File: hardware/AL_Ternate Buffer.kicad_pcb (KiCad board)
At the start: 2 copper layers, 45.7 x 71.1 mm, 0 parts

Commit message: Cursory start to layout.
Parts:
- added BT1: 9V, Connector_PinHeader_2.54mm:PinHeader_2x01_P2.54mm_Vertical, F.Cu at (77.9, 117.6)
- added C1: 47u 35V 20%, Capacitor_SMD:C_2220_5750Metric_Pad1.97x5.40mm_HandSolder, F.Cu at (69.9, 61.4)
- added C10: 100p 50V 5%, Capacitor_SMD:C_0805_2012Metric_Pad1.18x1.45mm_HandSolder, F.Cu at (82.8, 107.8)
- added C11: 100n 100V 10%, Capacitor_SMD:C_0805_2012Metric_Pad1.18x1.45mm_HandSolder, F.Cu at (82.8, 110.8)
- added C12: 100n 100V 10%, Capacitor_SMD:C_0805_2012Metric_Pad1.18x1.45mm_HandSolder, F.Cu at (82.8, 113.8)
- added C13: 10u 25V 10%, Capacitor_SMD:C_0805_2012Metric_Pad1.18x1.45mm_HandSolder, F.Cu at (87.6, 104.8)
- added C14: 10u 25V 10%, Capacitor_SMD:C_0805_2012Metric_Pad1.18x1.45mm_HandSolder, F.Cu at (87.6, 107.8)
- added C15: 10u 25V 10%, Capacitor_SMD:C_0805_2012Metric_Pad1.18x1.45mm_HandSolder, F.Cu at (87.6, 110.8)
- added C16: 10u 25V 10%, Capacitor_SMD:C_0805_2012Metric_Pad1.18x1.45mm_HandSolder, F.Cu at (87.6, 113.8)
- added C17: 10u 75V 10%, Capacitor_SMD:C_1210_3225Metric_Pad1.33x2.70mm_HandSolder, F.Cu at (77.3, 79.0)
- added C18: 10u 75V 10%, Capacitor_SMD:C_1210_3225Metric_Pad1.33x2.70mm_HandSolder, F.Cu at (77.3, 83.3)
- added C2: 47u 35V 20%, Capacitor_SMD:C_2220_5750Metric_Pad1.97x5.40mm_HandSolder, F.Cu at (69.9, 68.3)
- added C3: 47u 35V 20%, Capacitor_SMD:C_2220_5750Metric_Pad1.97x5.40mm_HandSolder, F.Cu at (69.9, 75.3)
- added C4: 10u 25V 10%, Capacitor_SMD:C_0805_2012Metric_Pad1.18x1.45mm_HandSolder, F.Cu at (78.0, 104.8)
- added C5: 1u 50V 10%, Capacitor_SMD:C_0805_2012Metric_Pad1.18x1.45mm_HandSolder, F.Cu at (78.0, 107.8)
- added C6: 47u 35V 20%, Capacitor_SMD:C_2220_5750Metric_Pad1.97x5.40mm_HandSolder, F.Cu at (69.9, 82.2)
- added C7: 10u 25V 10%, Capacitor_SMD:C_0805_2012Metric_Pad1.18x1.45mm_HandSolder, F.Cu at (78.0, 110.8)
- added C8: 1u 50V 10%, Capacitor_SMD:C_0805_2012Metric_Pad1.18x1.45mm_HandSolder, F.Cu at (78.0, 113.8)
- added C9: 100p 50V 5%, Capacitor_SMD:C_0805_2012Metric_Pad1.18x1.45mm_HandSolder, F.Cu at (82.8, 104.8)
- added D1: S3GHE3_A/I, Diode_SMD:D_SMB-SMC_Universal_Handsoldering, F.Cu at (82.1, 89.6)
- added D2: S3GHE3_A/I, Diode_SMD:D_SMB-SMC_Universal_Handsoldering, F.Cu at (82.1, 97.3)
- added D3: QBL8IW60D-NW, LED_THT:LED_D5.0mm, F.Cu at (82.8, 80.6)
- added H1: MountingHole_Pad, MountingHole:MountingHole_2.7mm_M2.5_Pad, F.Cu at (62.0, 61.4)
- added H2: MountingHole_Pad, MountingHole:MountingHole_2.7mm_M2.5_Pad, F.Cu at (62.0, 68.3)
- added H3: MountingHole_Pad, MountingHole:MountingHole_2.7mm_M2.5_Pad, F.Cu at (62.0, 75.3)
- added H4: MountingHole_Pad, MountingHole:MountingHole_2.7mm_M2.5_Pad, F.Cu at (62.0, 82.2)
- added J1: FC68148, Connector_BarrelJack:BarrelJack_Horizontal, F.Cu at (73.1, 108.7)
- added J2: NMJ6HCD2, Connector_Audio:Jack_6.35mm_Neutrik_NMJ6HCD2_Horizontal, F.Cu at (138.5, 76.7)
- added J3: NMJ6HCD2, Connector_Audio:Jack_6.35mm_Neutrik_NMJ6HCD2_Horizontal, F.Cu at (151.0, 82.1)
- added J4: NMJ6HCD2, Connector_Audio:Jack_6.35mm_Neutrik_NMJ6HCD2_Horizontal, F.Cu at (151.0, 103.6)
- added R1: 750, Resistor_SMD:R_0603_1608Metric_Pad0.98x0.95mm_HandSolder, F.Cu at (60.7, 87.0)
- added R10: 1M 1%, Resistor_SMD:R_0603_1608Metric_Pad0.98x0.95mm_HandSolder, F.Cu at (65.1, 92.0)
- added R11: 1k 1%, Resistor_SMD:R_0603_1608Metric_Pad0.98x0.95mm_HandSolder, F.Cu at (65.1, 94.5)
- added R12: 1k 1%, Resistor_SMD:R_0603_1608Metric_Pad0.98x0.95mm_HandSolder, F.Cu at (65.1, 97.0)
- added R13: 1M 1%, Resistor_SMD:R_0603_1608Metric_Pad0.98x0.95mm_HandSolder, F.Cu at (65.1, 99.5)
- added R14: 10k 0.5%, Resistor_SMD:R_0603_1608Metric_Pad0.98x0.95mm_HandSolder, F.Cu at (65.1, 102.0)
- added R15: 10k 0.5%, Resistor_SMD:R_0603_1608Metric_Pad0.98x0.95mm_HandSolder, F.Cu at (69.4, 87.0)
- added R16: 10k 0.5%, Resistor_SMD:R_0603_1608Metric_Pad0.98x0.95mm_HandSolder, F.Cu at (69.4, 89.5)
- added R17: 10k 0.5%, Resistor_SMD:R_0603_1608Metric_Pad0.98x0.95mm_HandSolder, F.Cu at (69.4, 92.0)
- added R18: 0, Resistor_SMD:R_0603_1608Metric_Pad0.98x0.95mm_HandSolder, F.Cu at (69.4, 94.5)
- added R19: 10k 0.5%, Resistor_SMD:R_0603_1608Metric_Pad0.98x0.95mm_HandSolder, F.Cu at (69.4, 97.0)
- added R2: 100 5%, Resistor_SMD:R_0603_1608Metric_Pad0.98x0.95mm_HandSolder, F.Cu at (60.7, 89.5)
- added R20: 10k 0.5%, Resistor_SMD:R_0603_1608Metric_Pad0.98x0.95mm_HandSolder, F.Cu at (69.4, 99.5)
- added R21: 0, Resistor_SMD:R_0603_1608Metric_Pad0.98x0.95mm_HandSolder, F.Cu at (69.4, 102.0)
- added R22: 10k 0.5%, Resistor_SMD:R_0603_1608Metric_Pad0.98x0.95mm_HandSolder, F.Cu at (73.8, 87.0)
- added R23: 10k 0.5%, Resistor_SMD:R_0603_1608Metric_Pad0.98x0.95mm_HandSolder, F.Cu at (73.8, 89.5)
- added R24: 10k 0.5%, Resistor_SMD:R_0603_1608Metric_Pad0.98x0.95mm_HandSolder, F.Cu at (73.8, 92.0)
- added R25: 10k 0.5%, Resistor_SMD:R_0603_1608Metric_Pad0.98x0.95mm_HandSolder, F.Cu at (73.8, 94.5)
- added R3: 100 5%, Resistor_SMD:R_0603_1608Metric_Pad0.98x0.95mm_HandSolder, F.Cu at (60.7, 92.0)
- added R4: 10k 0.5%, Resistor_SMD:R_0603_1608Metric_Pad0.98x0.95mm_HandSolder, F.Cu at (60.7, 94.5)
- added R5: 10k 0.5%, Resistor_SMD:R_0603_1608Metric_Pad0.98x0.95mm_HandSolder, F.Cu at (60.7, 97.0)
- added R6: 10k 0.5%, Resistor_SMD:R_0603_1608Metric_Pad0.98x0.95mm_HandSolder, F.Cu at (60.7, 99.5)
- added R7: 10k 0.5%, Resistor_SMD:R_0603_1608Metric_Pad0.98x0.95mm_HandSolder, F.Cu at (60.7, 102.0)
- added R8: 1k 1%, Resistor_SMD:R_0603_1608Metric_Pad0.98x0.95mm_HandSolder, F.Cu at (65.1, 87.0)
- added R9: 1k 1%, Resistor_SMD:R_0603_1608Metric_Pad0.98x0.95mm_HandSolder, F.Cu at (65.1, 89.5)
- added RV1: 10k A, Potentiometer_THT:Potentiometer_Runtron_RM-065_Vertical, F.Cu at (75.9, 70.4)
- added RV2: 10k A, Potentiometer_THT:Potentiometer_Runtron_RM-065_Vertical, F.Cu at (84.0, 70.4)
- added SW1: 7101SYZQE, Connector_PinHeader_2.54mm:PinHeader_1x03_P2.54mm_Vertical, F.Cu at (85.1, 60.2)
- added U1: OPA1664AIDR, Package_SO:SOIC-14_3.9x8.7mm_P1.27mm, F.Cu at (78.5, 63.2)

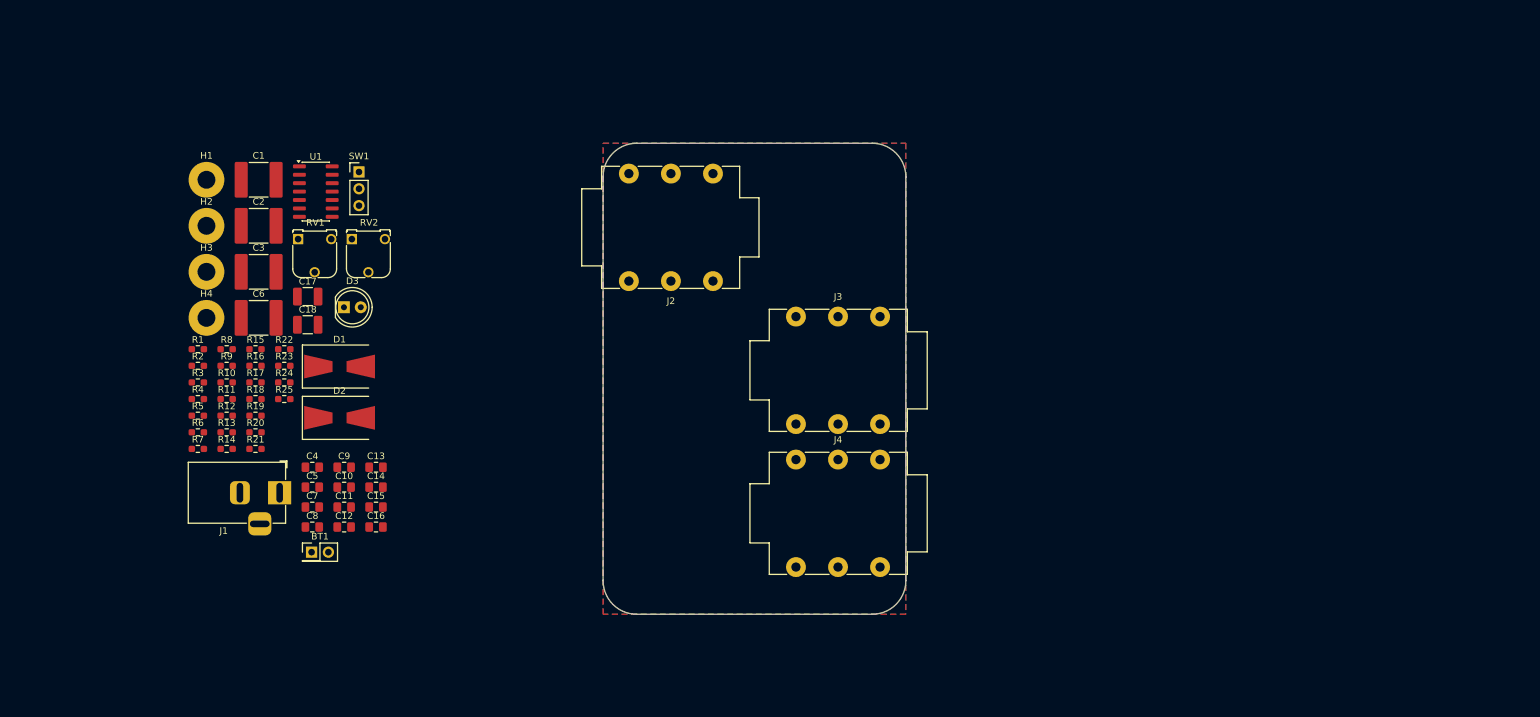
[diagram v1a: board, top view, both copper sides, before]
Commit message: Loose component grouping.
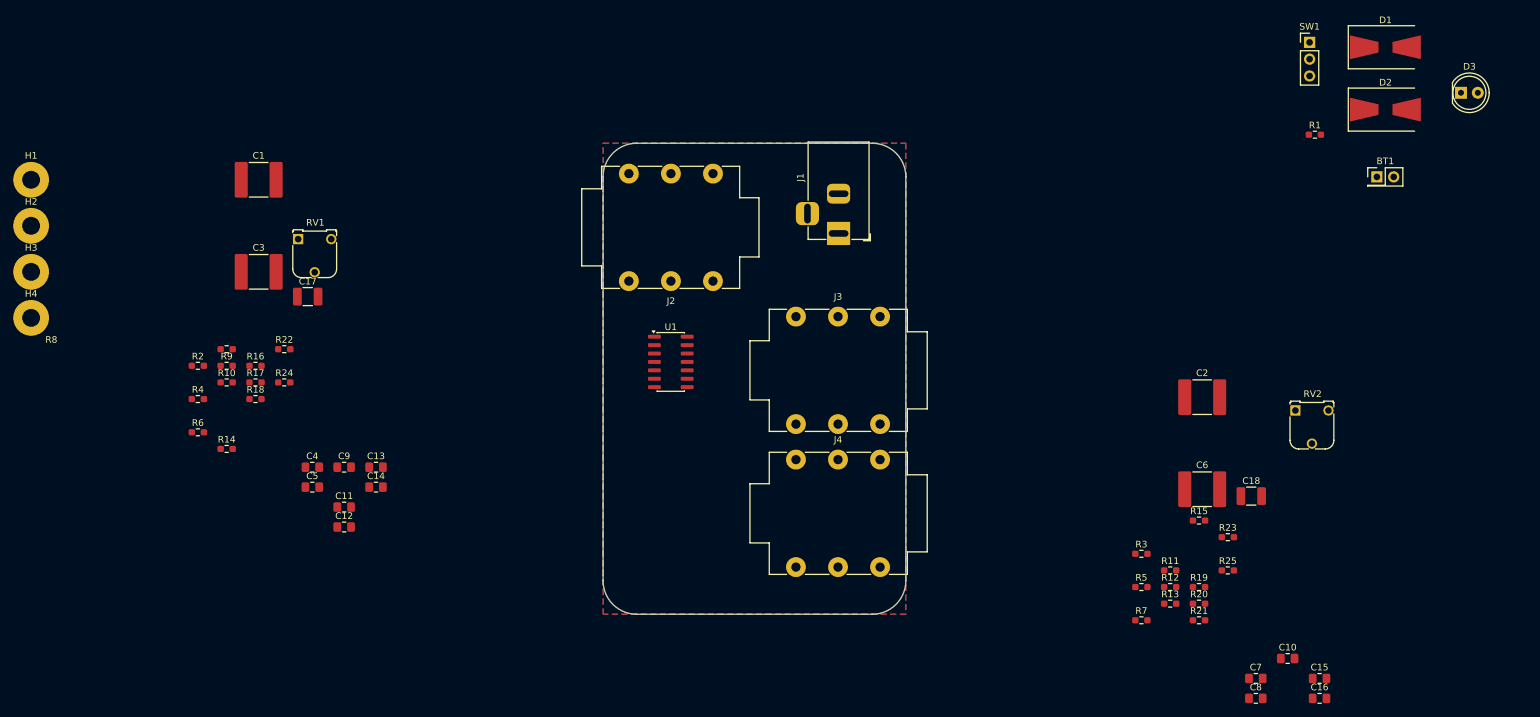
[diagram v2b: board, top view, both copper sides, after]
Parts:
- moved D3 171.7 mm to (251.5, 48.3)
- moved R1 171.7 mm to (229.4, 54.6)
- moved BT1 170.5 mm to (238.8, 61.0)
- moved D1 165.1 mm to (240.1, 41.4)
- moved D2 164.6 mm to (240.1, 50.8)
- moved SW1 144.9 mm to (228.6, 40.6)
- moved R11 144.8 mm to (207.6, 120.4)
- moved R12 144.8 mm to (207.6, 122.9)
- moved R13 144.8 mm to (207.6, 125.4)
- moved R15 144.8 mm to (211.9, 112.8)
- moved R19 144.8 mm to (211.9, 122.9)
- moved R20 144.8 mm to (211.9, 125.4)
- moved R21 144.8 mm to (211.9, 127.9)
- moved R23 144.8 mm to (216.3, 115.4)
- moved R25 144.8 mm to (216.3, 120.4)
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
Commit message: Caught error regarding op-amp polarity. Partial routing/placement progress.
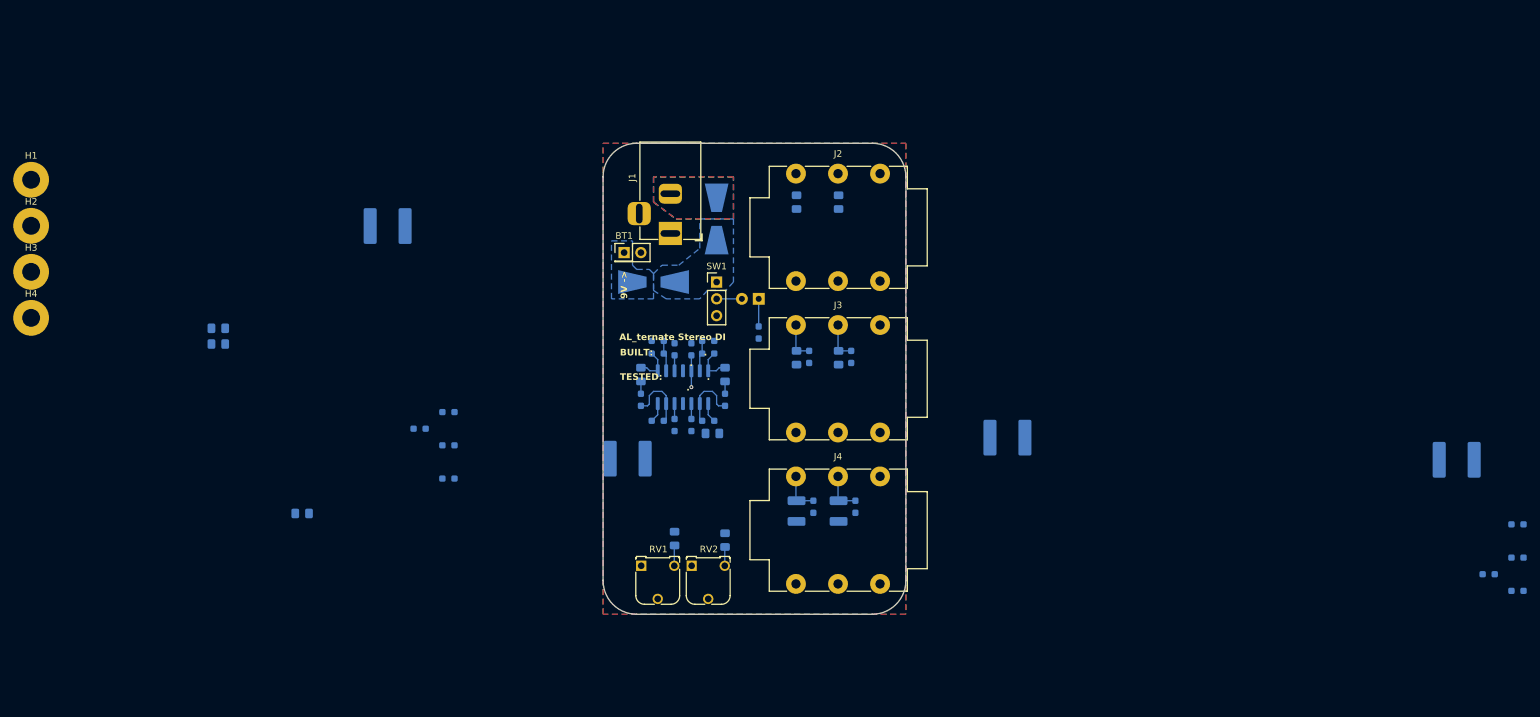
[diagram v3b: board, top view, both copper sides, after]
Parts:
- C1, C10, C11, C12, C13, C14, C15, C16, C17, C18, C2, C3, C4, C5, C6, C7, C8, C9, D1, D2, D3, R1, R10, R11, R12, R13, R14, R15, R16, R17, R18, R19, R2, R20, R21, R22, R23, R24, R25, R3, R4, R5, R6, R7, R8, R9, U1: moved to B.Cu
- moved D1 116.1 mm to (129.5, 76.8), turned to 180 degrees
- moved BT1 114.2 mm to (125.1, 72.4)
- moved D3 110.5 mm to (145.4, 79.4), turned to 180 degrees
- moved D2 102.3 mm to (139.1, 67.3), turned to 90 degrees
- moved C16 102.2 mm to (140.3, 90.8), turned to -90 degrees
- moved C8 102.1 mm to (151.1, 64.8), turned to -90 degrees
- moved SW1 96.6 mm to (139.1, 76.8)
- moved RV2 94.1 mm to (135.3, 119.7)
- moved C10 93.3 mm to (138.4, 99.7), turned to 180 degrees
- moved C15 92.6 mm to (151.1, 88.3), turned to 90 degrees
- moved C5 90.4 mm to (157.5, 64.8), turned to -90 degrees
- moved R16 90.0 mm to (159.4, 88.1), turned to -90 degrees
- moved R1 89.1 mm to (145.4, 84.5), turned to -90 degrees
- moved R24 88.3 mm to (160.0, 110.8), turned to -90 degrees
- moved C17 86.4 mm to (157.5, 111.4), turned to 90 degrees
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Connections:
- C10 pad 1: Net-(U1B--) -> Net-(U1B-+)
- R11 pad 2: Net-(U1B-+) -> Net-(U1B--)
- R12 pad 2: Net-(U1B--) -> Net-(U1B-+)
- R13 pad 1: Net-(U1B--) -> Net-(U1B-+)
- R15 pad 1: Net-(U1B-+) -> Net-(U1B--)
- R17 pad 2: Net-(U1D-+) -> Net-(U1D--)
- R18 pad 2: Net-(U1D--) -> Net-(U1D-+)
- R20 pad 2: Net-(U1C-+) -> Net-(U1C--)
- R21 pad 2: Net-(U1C--) -> Net-(U1C-+)
- R22 pad 1: Net-(U1D-+) -> Net-(U1D--)
- R23 pad 1: Net-(U1C-+) -> Net-(U1C--)
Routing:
- net Net-(U1C--): track 0.00 -> 9.68 mm
- net Net-(U1D--): track 0.00 -> 9.68 mm
- net /OUT 2 - STEREO: track 0.00 -> 6.25 mm
- net /OUT 2 - MONO: track 0.00 -> 6.25 mm
- net /OUT 1 - MONO: track 0.00 -> 5.84 mm
- net /OUT 1 - STEREO: track 0.00 -> 5.84 mm
- net Net-(C15-Pad1): track 0.00 -> 5.72 mm
- net Net-(C13-Pad1): track 0.00 -> 5.72 mm
- net Net-(U1B-+): track 0.00 -> 4.80 mm, vias 0 -> 1
- net Net-(U1B--): track 0.00 -> 4.66 mm
- net Net-(U1A--): track 0.00 -> 4.66 mm
- net Net-(D3-K): track 0.00 -> 4.17 mm
- net VCC: track 0.00 -> 3.81 mm
- net Net-(C4-Pad1): track 0.00 -> 3.03 mm
- net Net-(C18-Pad1): track 0.00 -> 2.98 mm
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- added copper zone on B.Cu, net +BATT
- added copper zone on B.Cu, net Net-(D1-K)
- added copper zone on B.Cu, net VIN
- added copper zone on F.Cu, net VIN
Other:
- board text added: "9V ->"

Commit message: Further routing.
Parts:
- C11, C12: moved to F.Cu
- moved R13 121.8 mm to (135.3, 102.2), turned to 90 degrees
- moved R7 121.3 mm to (141.6, 97.2), turned to 0 degrees
- moved R5 120.0 mm to (141.6, 99.1)
- moved R3 117.8 mm to (142.9, 101.0)
- moved C6 110.1 mm to (141.0, 111.8), turned to 0 degrees
- moved C11 71.4 mm to (135.3, 85.3), turned to 0 degrees
- moved C12 71.4 mm to (135.3, 87.7), turned to 0 degrees
- moved C9 54.2 mm to (129.5, 101.0), turned to 0 degrees
- moved C1 52.8 mm to (127.0, 105.4)
- moved C2 42.3 mm to (141.0, 105.4), turned to 0 degrees
- moved R10 38.6 mm to (132.7, 102.2), turned to 90 degrees
- moved R6 29.3 mm to (126.4, 97.2)
- moved R4 27.9 mm to (126.4, 99.1), turned to 0 degrees
- moved R2 26.9 mm to (125.1, 101.0), turned to 0 degrees
- moved C3 8.37 mm to (127.0, 111.8)
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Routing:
- net Net-(C3-Pad1): track 0.00 -> 24.0 mm
- net Net-(C10-Pad2): track 0.00 -> 23.4 mm
- net Net-(C15-Pad1): track 5.72 -> 16.7 mm
- net Net-(C2-Pad1): track 0.00 -> 8.76 mm
- net Net-(C1-Pad1): track 0.00 -> 8.66 mm
- net Net-(U1A-+): track 2.33 -> 9.97 mm, vias 0 -> 1
- net Net-(U1B-+): track 4.80 -> 7.44 mm, vias 1 -> 0

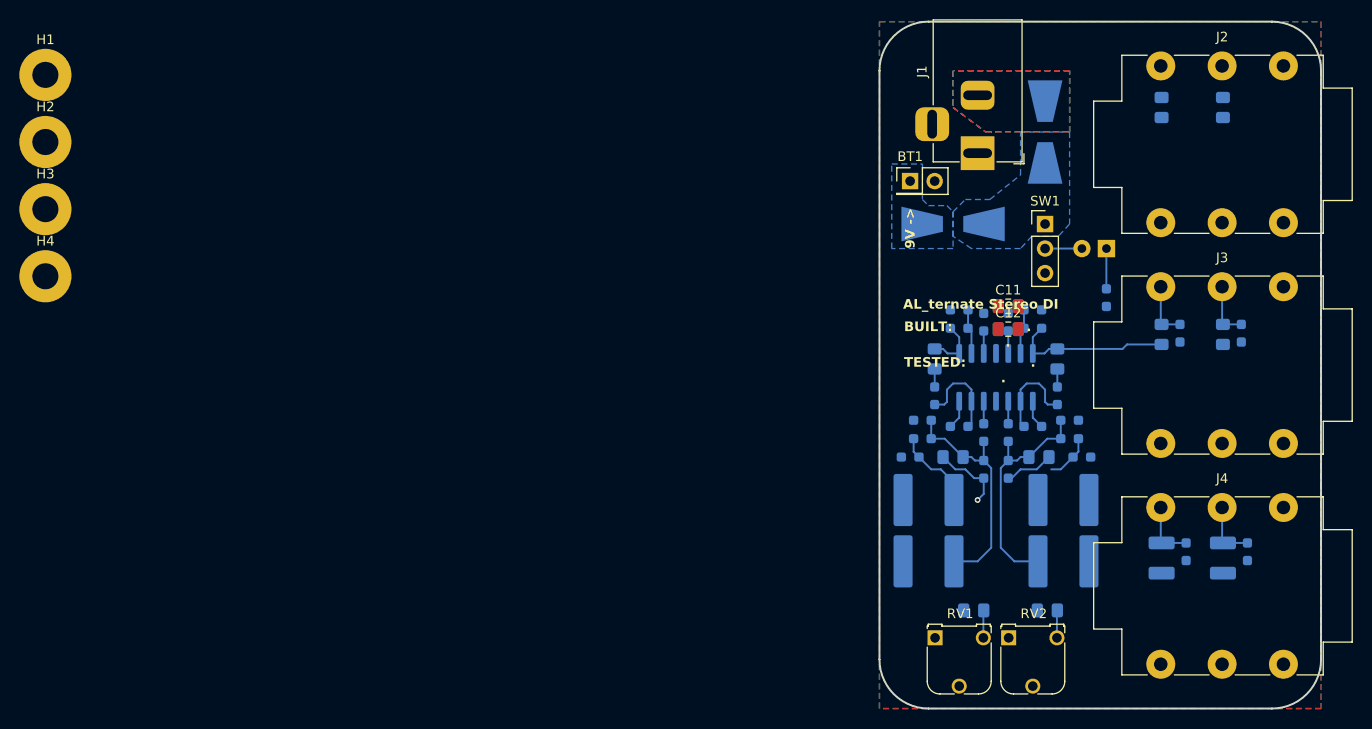
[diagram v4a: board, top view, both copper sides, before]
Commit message: Finished tentative routing.
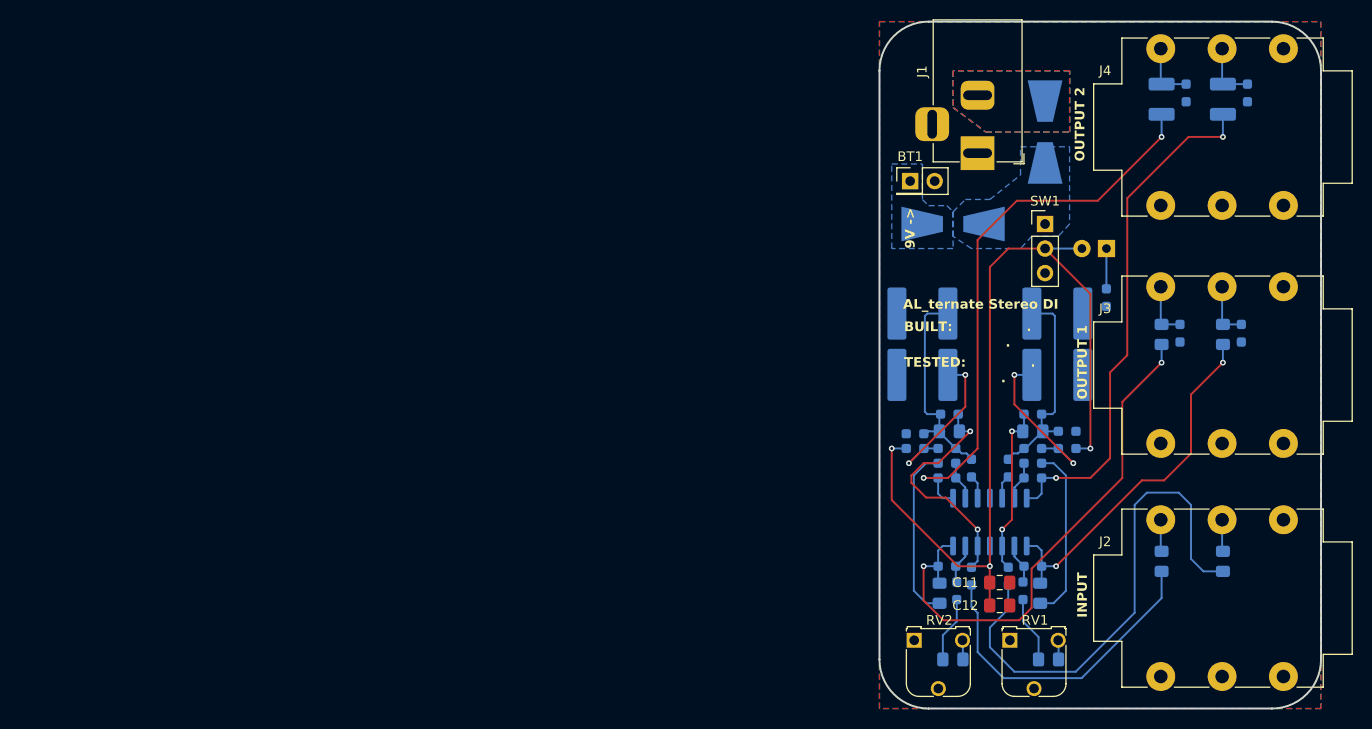
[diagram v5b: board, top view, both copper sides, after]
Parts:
- removed H1, H2, H3, H4: MountingHole_Pad, MountingHole:MountingHole_2.7mm_M2.5_Pad
- moved C17 47.5 mm to (157.5, 63.9)
- moved C18 47.5 mm to (151.1, 63.9)
- moved J4 47.5 mm to (151.0, 58.7)
- moved R24 47.5 mm to (160.0, 63.3)
- moved R25 47.5 mm to (153.7, 63.3)
- moved C5 47.0 mm to (157.5, 111.8)
- moved C8 47.0 mm to (151.1, 111.8)
- moved J2 47.0 mm to (151.0, 107.5)
- moved R11 30.1 mm to (129.9, 114.8), turned to 90 degrees
- moved R8 29.8 mm to (136.8, 114.8), turned to 90 degrees
- moved C6 29.5 mm to (126.4, 86.1), turned to 180 degrees
- moved C3 28.9 mm to (140.3, 86.1), turned to 0 degrees
- moved C11 28.6 mm to (134.4, 114.0)
- moved C12 28.6 mm to (134.4, 116.3)
- moved C16 27.1 mm to (128.1, 115.1)
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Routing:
- net VCC: track 3.81 -> 91.5 mm, vias 0 -> 3
- net Net-(C18-Pad1): track 2.98 -> 59.1 mm, vias 0 -> 2
- net Net-(C5-Pad2): track 0.00 -> 53.3 mm
- net Net-(C17-Pad1): track 2.98 -> 53.8 mm, vias 0 -> 2
- net Net-(C15-Pad1): track 16.7 -> 55.6 mm, vias 0 -> 2
- net Net-(C8-Pad2): track 0.00 -> 33.6 mm
- net Net-(C13-Pad1): track 5.72 -> 38.1 mm, vias 0 -> 2
- net Net-(U1B-+): track 7.44 -> 24.7 mm, vias 0 -> 2
- net Net-(C16-Pad2): track 1.86 -> 18.2 mm
- net Net-(C14-Pad2): track 1.86 -> 18.2 mm
- net Net-(C1-Pad1): track 8.66 -> 17.4 mm, vias 0 -> 2
- net Net-(C2-Pad1): track 8.76 -> 17.0 mm, vias 0 -> 2
- net Net-(U1A-+): track 9.97 -> 17.7 mm, vias 1 -> 2
- net Net-(C4-Pad2): track 0.00 -> 6.87 mm
- net Net-(C7-Pad2): track 0.00 -> 6.80 mm
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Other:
- board text added: "<- 9V"
- board text added: "INPUT"
- board text added: "OUTPUT 1"
- board text added: "OUTPUT 2"
